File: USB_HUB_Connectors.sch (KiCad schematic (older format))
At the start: 52 parts

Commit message: Added footprint of 2x USB-A stacked. Added connections to USB HUB.
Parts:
- added D?: 1N4148WS, sc606-baseboard-footprints:SOD-323F, symbol sc606-baseboard:1N4148WS
- added FB?: BLM18EG221SN1D, sc606-baseboard-footprints:0603, symbol sc606-baseboard:BLM18EG221SN1D
- added TP? (x4): TP_SMD_0_75MM-antmicroTestPoints, sc606-baseboard-footprints:Testpoint_smd_0_75mm, symbol sc606-baseboard:TP_SMD_0_75MM-antmicroTestPoints
- added U? (x2): GSB3112311HR, sc606-baseboard-footprints:GSB3112311HR, symbol sc606-baseboard:GSB3112311HR
- C? (x2): footprint antmicro-footprints:0402-cap -> sc606-baseboard-footprints:0402-cap; symbol antmicroCapacitors0402:C_1u_0402 -> sc606-baseboard:C_1u_0402
- C? (x2): footprint antmicro-footprints:0402-cap -> sc606-baseboard-footprints:0402-cap; symbol antmicroCapacitors0402:C_10u_0402 -> sc606-baseboard:C_10u_0402
- R? (x5): footprint antmicro-footprints:0402-res -> sc606-baseboard-footprints:0402-res; symbol antmicroResistors0402:R_20k_0402 -> sc606-baseboard:R_20k_0402
- R?: footprint antmicro-footprints:0603-res -> sc606-baseboard-footprints:0603-res; symbol antmicroResistors0603:R_12k_1%_0603 -> sc606-baseboard:R_12k_1%_0603
- R?: footprint antmicro-footprints:0402-res -> sc606-baseboard-footprints:0402-res; symbol antmicroResistors0402:R_0R_0402 -> sc606-baseboard:R_0R_0402
- R?: footprint antmicro-footprints:0402-res -> sc606-baseboard-footprints:0402-res; symbol antmicroResistors0402:R_1M0_0402 -> sc606-baseboard:R_1M0_0402
- R? (x2): footprint antmicro-footprints:0402-res -> sc606-baseboard-footprints:0402-res; symbol antmicroResistors0402:R_200k_0402 -> sc606-baseboard:R_200k_0402
- TP?: footprint antmicro-footprints:Testpoint_smd_0_75mm -> sc606-baseboard-footprints:Testpoint_smd_0_75mm; symbol sc606-baseboard-rescue:TP_SMD_0_75MM-antmicroTestPoints -> sc606-baseboard:TP_SMD_0_75MM-antmicroTestPoints
- U?: footprint antmicro-footprints:QFN40P700X700X100-57N -> sc606-baseboard-footprints:QFN40P700X700X100-57N; symbol antmicroInterfaceControllers:USB57442G -> sc606-baseboard:USB57442G
- Y?: footprint antmicro-footprints:KX-7 -> sc606-baseboard-footprints:KX-7; symbol antmicroCrystals:ABM8G-25.000MHZ-B4Y-T -> sc606-baseboard:ABM8G-25.000MHZ-B4Y-T
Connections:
- net labels added: 5V0_SYS, 5V0_USB, USB_1_D_N, USB_1_D_P
- net labels removed: USBC_VBUS
- wire segments 143 -> 164
- no-connect marks 3 -> 1
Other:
- note added: "2x USB-A Stack connector"
- note added: "rozłożyć elementy na płytce i sprawdzić, czy dodamy drugi USB-C.\nWtedy trzeba robić switch.\nJak nie, to RX/TX2 podpinamy pod osobny port."
- moved on the sheet: C?, D?, J?, R?, TP?

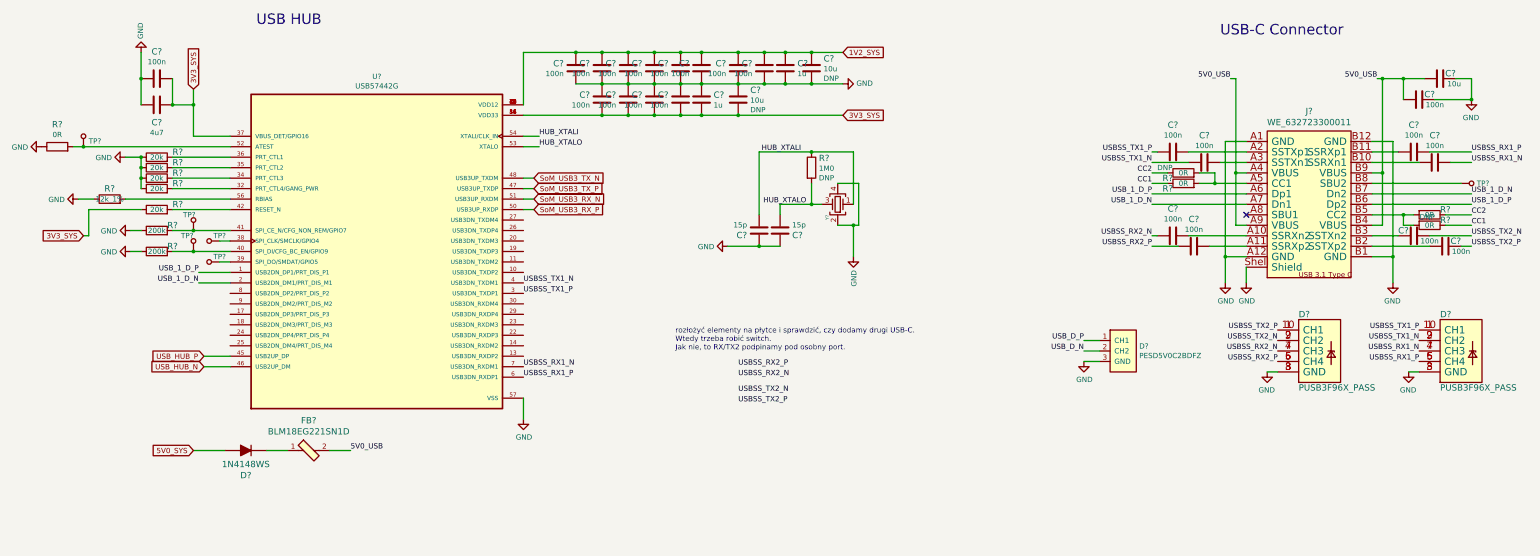
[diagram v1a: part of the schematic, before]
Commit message: Started placing main components on PCB. Change of RT battery model and USB flash connector
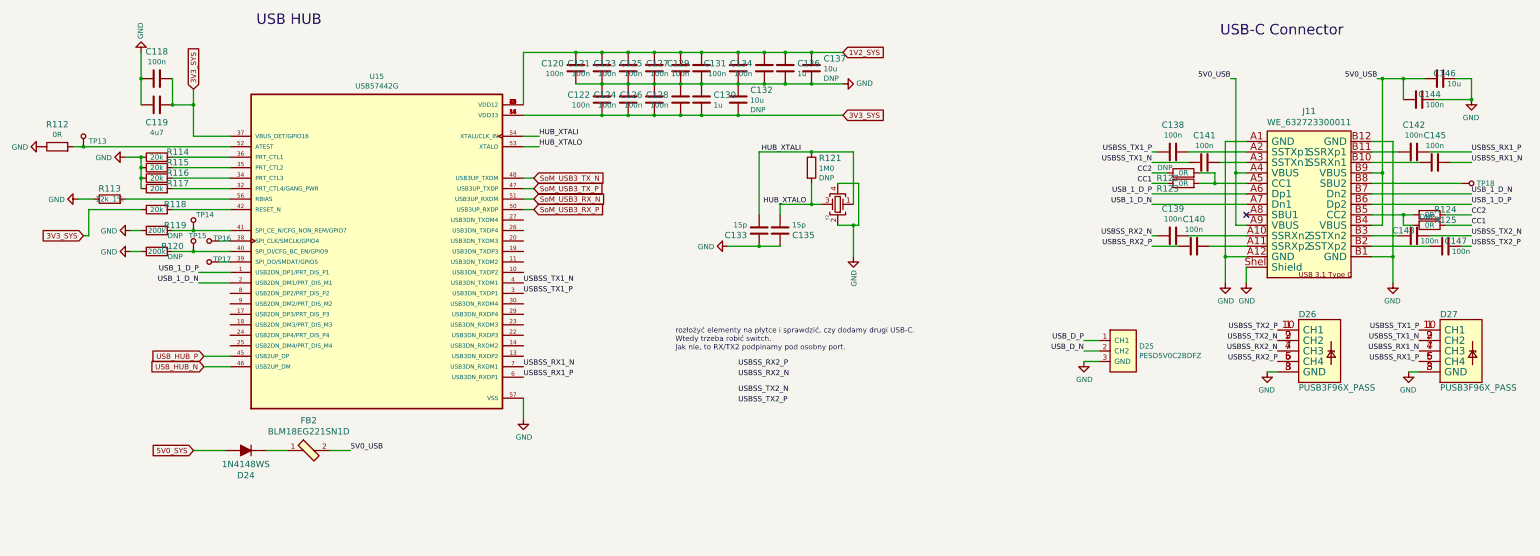
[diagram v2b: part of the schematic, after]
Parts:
- R119, R120: renamed from R?; DNP (none) -> DNP
- gave numbers to parts that had none: 57

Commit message: Added USB A and C double stack connector
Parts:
- removed C139, C140, C142, C143, C144, C145, C147: C_100n_0402, sc606-baseboard-footprints:0402-cap, symbol sc606-baseboard:C_100n_0402
- removed C146: C_10u_0402, sc606-baseboard-footprints:0402-cap, symbol sc606-baseboard:C_10u_0402
- removed J11: WE_632723300011, sc606-baseboard-footprints:WE_632723300011, symbol sc606-baseboard:WE_632723300011
- removed R124, R125: R_0R_0402, sc606-baseboard-footprints:0402-res, symbol sc606-baseboard:R_0R_0402
- removed TP18: TP_SMD_0_75MM, sc606-baseboard-footprints:Testpoint_smd_0_75mm, symbol sc606-baseboard:TP_SMD_0_75MM
- removed U14: GSB3112311HR, sc606-baseboard-footprints:GSB3112311HR, symbol sc606-baseboard:GSB3112311HR
- added C? (x7): C_100n_0402, sc606-baseboard-footprints:0402-cap, symbol sc606-baseboard:C_100n_0402
- added C?: C_10u_0402, sc606-baseboard-footprints:0402-cap, symbol sc606-baseboard:C_10u_0402
- added J? (x2): USB-A3-C31-D-RA-CS1, antmicro-footprints:USB-A3-C31-D-RA-CS1, symbol antmicroUSBDVIHDMIConnectors:USB-A3-C31-D-RA-CS1
- added R? (x2): R_0R_0402, sc606-baseboard-footprints:0402-res, symbol sc606-baseboard:R_0R_0402
- added TP? (x2): TP_SMD_0_75MM, sc606-baseboard-footprints:Testpoint_smd_0_75mm, symbol sc606-baseboard:TP_SMD_0_75MM
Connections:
- net labels added: USB_A1_D_N, USB_A1_D_P, USB_A1_SS_RX_N, USB_A1_SS_RX_P, USB_A1_SS_TX_N, USB_A1_SS_TX_P, USB_C1A_D_N, USB_C1A_D_P, USB_C1B_D_N, USB_C1B_D_P, USB_C1_CC1, USB_C1_CC2, USB_C1_SS_RX1_N, USB_C1_SS_RX1_P, USB_C1_SS_RX2_N, USB_C1_SS_RX2_P, USB_C1_SS_TX1_N, USB_C1_SS_TX1_P, USB_C1_SS_TX2_N, USB_C1_SS_TX2_P
- net labels removed: CC1, CC2
- wire segments 164 -> 153
- no-connect marks 1 -> 0
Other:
- note added: "2x USB-A and USB-C Stack connector"
- note removed: "2x USB-A Stack connector"
- note removed: "USB-C Connector"
- note removed: "rozłożyć elementy na płytce i sprawdzić, czy dodamy drugi USB-C.\nWtedy trzeba robić switch.\nJak nie, to RX/TX2 podpinamy pod osobny port."
- moved on the sheet: C138, C141, D25, D26, D27, R122, R123

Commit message: Added connections of both USB A & C connectors
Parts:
- removed D25: PESD5V0C2BDFZ, sc606-baseboard-footprints:DFN0603-3, symbol sc606-baseboard:PESD5V0C2BDFZ
- added C? (x11): C_100n_0402, sc606-baseboard-footprints:0402-cap, symbol sc606-baseboard:C_100n_0402
- added C? (x2): C_47u_0603, antmicro-footprints:0603-cap, symbol antmicroCapacitors0603:C_47u_0603
- added C?: C_10u_0402, sc606-baseboard-footprints:0402-cap, symbol sc606-baseboard:C_10u_0402
- added D? (x6): PUSB3F96X_PASS, sc606-baseboard-footprints:PUSB3F96X, symbol sc606-baseboard:PUSB3F96X_PASS
- added IC? (x2): HD3SS3220, antmicro-footprints:RNH0030A, symbol antmicroInterfaceControllers:HD3SS3220
- added J? (x2): USB-A3-C31-D-RA-CS1, antmicro-footprints:USB-A3-C31-D-RA-CS1, symbol antmicroUSBDVIHDMIConnectors:USB-A3-C31-D-RA-CS1
- added R? (x2): R_909k_0402, antmicro-footprints:0402-res, symbol antmicroResistors0402:R_909k_0402
- added R? (x4): R_200k_0402, antmicro-footprints:0402-res, symbol antmicroResistors0402:R_200k_0402
- added R? (x2): R_10k_0402, antmicro-footprints:0402-res, symbol antmicroResistors0402:R_10k_0402
- added R? (x6): R_2k_0402, antmicro-footprints:0402-res, symbol antmicroResistors0402:R_2k_0402
- added R? (x14): R_0R_0402, antmicro-footprints:0402-res, symbol antmicroResistors0402:R_0R_0402
- added R? (x4): R_0R_0402, sc606-baseboard-footprints:0402-res, symbol sc606-baseboard:R_0R_0402
- added TP? (x8): TP_SMD_0_75MM, sc606-baseboard-footprints:Testpoint_smd_0_75mm, symbol sc606-baseboard:TP_SMD_0_75MM
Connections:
- net USBSS_RX1_N is gone; now on net USB_C1_SS_TX2_P: D27.4 (CH3), D27.7 (CH3)
- net USBSS_RX1_P is gone; now on net USB_C1_SS_TX2_N: D27.5 (CH4), D27.6 (CH4)
- net USBSS_RX2_N is gone; now on net USB_A1_D_N: D26.4 (CH3), D26.7 (CH3)
- net USBSS_RX2_P is gone; now on net USB_A1_D_P: D26.5 (CH4), D26.6 (CH4)
- net USBSS_TX1_N is gone; now on net USB_C1_SS_RX2_N: D27.2 (CH2), D27.9 (CH2)
- net USBSS_TX1_P is gone; now on net USB_C1_SS_RX2_P: D27.1 (CH1), D27.10 (CH1)
- net USBSS_TX2_N is gone; now on net USB_C1_D_N: D26.2 (CH2), D26.9 (CH2)
- net USBSS_TX2_P is gone; now on net USB_C1_D_P: D26.1 (CH1), D26.10 (CH1)
- net USB_1_D_N is gone; now on net USB_A1_D_N: U15.2 (USB2DN_DM1/PRT_DIS_M1)
- net USB_1_D_P is gone; now on net USB_A1_D_P: U15.1 (USB2DN_DP1/PRT_DIS_P1)
- net USB_C1A_D_N is gone; now on net USB_C1_D_N: J?.A7 (DA-)
- net USB_C1A_D_P is gone; now on net USB_C1_D_P: J?.A6 (DA+)
- net USB_C1B_D_N is gone; now on net USB_C1_D_N: J?.B7 (DB-)
- net USB_C1B_D_P is gone; now on net USB_C1_D_P: J?.B6 (DB+)
- net 3V3_SYS: now also C?.2, C?.2, IC?.8 (VCC33), IC?.8 (VCC33), R?.1, R?.1, R?.1, R?.1, R?.2, R?.2
- net 5V0_SYS: now also C?.1, C?.1, IC?.30 (VDD5), IC?.30 (VDD5), R?.1, R?.1, R?.1, R?.1, R?.1, R?.1
- net 5V0_USB: now also C?.1, C?.2, J?.1 (VBUS), J?.A4 (VBUS), J?.A9 (VBUS), J?.B4 (VBUS), J?.B9 (VBUS), R?.1, R?.1
- net GND: now also C?.1, C?.1, C?.1, C?.2, C?.2, C?.2, D?.3 (GND), D?.3 (GND), D?.3 (GND), D?.3 (GND), D?.3 (GND), D?.3 (GND), D?.8 (GND), D?.8 (GND), D?.8 (GND), D?.8 (GND), D?.8 (GND), D?.8 (GND), IC?.13 (GND), IC?.13 (GND), IC?.28 (GND), IC?.28 (GND), IC?.31 (GND), IC?.31 (GND), J?.4 (GND), J?.7 (GNDDRAIN), J?.A1 (GND), J?.A12 (GND), J?.B1 (GND), J?.B12 (GND), R?.1, R?.1, R?.1, R?.1
- net SoM_USB3_RX_N: now also U15.48 (USB3UP_TXDM); no longer U15.51 (USB3UP_RXDM)
- net SoM_USB3_RX_P: now also U15.47 (USB3UP_TXDP); no longer U15.50 (USB3UP_RXDP)
- net SoM_USB3_TX_N: now also U15.51 (USB3UP_RXDM); no longer U15.48 (USB3UP_TXDM)
- net SoM_USB3_TX_P: now also U15.50 (USB3UP_RXDP); no longer U15.47 (USB3UP_TXDP)
- net USB_A1_SS_RX_N: now also U15.7 (USB3DN_RXDM1), D?.5 (CH4), D?.6 (CH4)
- net USB_A1_SS_RX_P: now also U15.6 (USB3DN_RXDP1), D?.4 (CH3), D?.7 (CH3)
- net USB_A1_SS_TX_N: now also U15.4 (USB3DN_TXDM1), D?.2 (CH2), D?.9 (CH2)
- net USB_A1_SS_TX_P: now also U15.3 (USB3DN_TXDP1), D?.1 (CH1), D?.10 (CH1)
- net USB_C1_CC1: now also IC?.2 (CC1)
- net USB_C1_CC2: now also IC?.1 (CC2)
- net USB_C1_SS_RX1_N: now also D?.5 (CH4), D?.6 (CH4), IC?.14 (RX1n)
- net USB_C1_SS_RX1_P: now also D?.4 (CH3), D?.7 (CH3), IC?.15 (RX1p)
- net USB_C1_SS_RX2_N: now also IC?.18 (RX2n)
- net USB_C1_SS_RX2_P: now also IC?.19 (RX2p)
- net USB_C1_SS_TX1_N: now also D?.2 (CH2), D?.9 (CH2), IC?.16 (TX1n)
- net USB_C1_SS_TX1_P: now also D?.1 (CH1), D?.10 (CH1), IC?.17 (TX1p)
- net USB_C1_SS_TX2_N: now also IC?.20 (TX2n)
- net USB_C1_SS_TX2_P: now also IC?.21 (TX2p)
- net USB_C1_SS_TX_P: now reaches U15.10 (USB3DN_TXDP2)
- net USB_C1_SS_TX_P: now also R?.1
- net USB_C1_SS_TX_N: now reaches U15.11 (USB3DN_TXDM2)
- net USB_C1_SS_TX_N: now also R?.1
- net USB_C1_SS_RX_P: now reaches U15.13 (USB3DN_RXDP2)
- net USB_C1_SS_RX_P: now also R?.1
- net USB_C1_SS_RX_N: now reaches U15.14 (USB3DN_RXDM2)
- net USB_C1_SS_RX_N: now also R?.1
- net USB_A2_D_P: now reaches U15.17 (USB2DN_DP3/PRT_DIS_P3)
- net USB_A2_D_P: now also D?.5 (CH4), D?.6 (CH4), J?.3 (D+)
- net USB_A2_D_N: now reaches U15.18 (USB2DN_DM3/PRT_DIS_M3)
- net USB_A2_D_N: now also D?.4 (CH3), D?.7 (CH3), J?.2 (D-)
- net USB_A2_SS_TX_P: now reaches U15.19 (USB3DN_TXDP3)
- net USB_A2_SS_TX_P: now also D?.1 (CH1), D?.10 (CH1), J?.9 (STDA_SSTX+)
- net USB_A2_SS_TX_N: now reaches U15.20 (USB3DN_TXDM3)
- net USB_A2_SS_TX_N: now also D?.2 (CH2), D?.9 (CH2), J?.8 (STDA_SSTX-)
- net USB_A2_SS_RX_P: now reaches U15.22 (USB3DN_RXDP3)
- net USB_A2_SS_RX_P: now also D?.4 (CH3), D?.7 (CH3), J?.6 (STDA_SSRX+)
- net USB_A2_SS_RX_N: now reaches U15.23 (USB3DN_RXDM3)
- net USB_A2_SS_RX_N: now also D?.5 (CH4), D?.6 (CH4), J?.5 (STDA_SSRX-)
- net USB_C2_D_P: now reaches U15.24 (USB2DN_DP4/PRT_DIS_P4)
- net USB_C2_D_P: now also D?.1 (CH1), D?.10 (CH1), J?.A6 (DA+), J?.B6 (DB+)
- net USB_C2_D_N: now reaches U15.25 (USB2DN_DM4/PRT_DIS_M4)
- net USB_C2_D_N: now also D?.2 (CH2), D?.9 (CH2), J?.A7 (DA-), J?.B7 (DB-)
- net USB_C2_SS_TX_P: now reaches U15.26 (USB3DN_TXDP4)
- net USB_C2_SS_TX_P: now also R?.1
- net USB_C2_SS_TX_N: now reaches U15.27 (USB3DN_TXDM4)
- net USB_C2_SS_TX_N: now also R?.1
- net USB_C2_SS_RX_P: now reaches U15.29 (USB3DN_RXDP4)
- net USB_C2_SS_RX_P: now also R?.1
- net USB_C2_SS_RX_N: now reaches U15.30 (USB3DN_RXDM4)
- net USB_C2_SS_RX_N: now also R?.1
- net USB_C1_D_P: now reaches U15.8 (USB2DN_DP2/PRT_DIS_P2)
- net USB_C1_D_N: now reaches U15.9 (USB2DN_DM2/PRT_DIS_M2)
- new net: IC?.10 (RXn), R?.2 (x2)
- new net: IC?.11 (DIR), R?.1 (x2)
- new net: IC?.22 (ADDR), TP?.1 (x2)
- new net: IC?.23 (INT_N/OUT3), R?.2 (x2)
- new net: IC?.24 (VCONN_FAULT_N), TP?.1 (x2)
- new net: IC?.25 (SDA/OUT1), R?.2 (x2)
- new net: IC?.26 (SCL/OUT2), R?.2 (x2)
- new net: IC?.29 (ENn_CC), R?.2 (x2)
- new net: IC?.3 (CURRENT_MODE), R?.2 (x2)
- new net: IC?.4 (PORT), R?.2 (x2)
- new net: IC?.5 (VBUS_DET), R?.2 (x2)
- new net: IC?.6 (TXp), R?.2 (x2)
- new net: IC?.7 (TXn), R?.2 (x2)
- new net: IC?.9 (RXp), R?.2 (x2)
- new net: J?.B5 (CC2), R?.2, R?.2
- new net: C?.1, J?.A2 (TX1+)
- new net: C?.1, J?.A3 (TX1-)
- new net: C?.1, J?.A10 (RX2-)
- new net: C?.1, J?.A11 (RX2+)
- new net: J?.A5 (CC1), R?.2, R?.2
- new net: J?.A8 (SBU1), TP?.1
- new net: C?.1, J?.B10 (RX1-)
- new net: C?.1, J?.B11 (RX1+)
- new net: C?.1, J?.B2 (TX2+)
- new net: C?.1, J?.B3 (TX2-)
- new net: J?.B8 (SBU2), TP?.1
- new net EN1_MUX: IC?.12 (ENn_MUX), R?.1, R?.2
- new net EN2_MUX: IC?.12 (ENn_MUX), R?.1, R?.2
- new net USBC1_ID: IC?.27 (ID), R?.2, TP?.1
- new net USBC2_ID: IC?.27 (ID), R?.2, TP?.1
- new net USB_C2_CC1: IC?.2 (CC1), R?.1, R?.1
- new net USB_C2_CC2: IC?.1 (CC2), R?.1, R?.1
- new net USB_C2_SS_RX1_N: C?.2, D?.5 (CH4), D?.6 (CH4), IC?.14 (RX1n)
- new net USB_C2_SS_RX1_P: C?.2, D?.4 (CH3), D?.7 (CH3), IC?.15 (RX1p)
- new net USB_C2_SS_RX2_N: C?.2, D?.2 (CH2), D?.9 (CH2), IC?.18 (RX2n)
- new net USB_C2_SS_RX2_P: C?.2, D?.1 (CH1), D?.10 (CH1), IC?.19 (RX2p)
- new net USB_C2_SS_TX1_N: C?.2, D?.2 (CH2), D?.9 (CH2), IC?.16 (TX1n)
- new net USB_C2_SS_TX1_P: C?.2, D?.1 (CH1), D?.10 (CH1), IC?.17 (TX1p)
- new net USB_C2_SS_TX2_N: C?.2, D?.5 (CH4), D?.6 (CH4), IC?.20 (TX2n)
- new net USB_C2_SS_TX2_P: C?.2, D?.4 (CH3), D?.7 (CH3), IC?.21 (TX2p)
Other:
- note added: "USB-A and USB-C Stack connector"
- note removed: "2x USB-A and USB-C Stack connector"
- moved on the sheet: C138, C141, C?, D26, D27, J?A, J?B, R122, R123, R?, TP?

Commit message: Main components placed on board
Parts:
- gave numbers to parts that had none: 76

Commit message: Main 5V buck converter placed and routed
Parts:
- C146, C158: footprint antmicro-footprints:0603-cap -> sc606-baseboard-footprints:0603-cap; symbol antmicroCapacitors0603:C_47u_0603 -> sc606-baseboard:C_47u_0603
- IC3, IC4: footprint antmicro-footprints:RNH0030A -> sc606-baseboard-footprints:RNH0030A; symbol antmicroInterfaceControllers:HD3SS3220 -> sc606-baseboard:HD3SS3220
- J11, J13: footprint antmicro-footprints:USB-A3-C31-D-RA-CS1 -> sc606-baseboard-footprints:USB-A3-C31-D-RA-CS1; symbol antmicroUSBDVIHDMIConnectors:USB-A3-C31-D-RA-CS1 -> sc606-baseboard:USB-A3-C31-D-RA-CS1
- R130, R142, R144, R160: footprint antmicro-footprints:0402-res -> sc606-baseboard-footprints:0402-res; symbol antmicroResistors0402:R_200k_0402 -> sc606-baseboard:R_200k_0402
- R131, R145: footprint antmicro-footprints:0402-res -> sc606-baseboard-footprints:0402-res; symbol antmicroResistors0402:R_10k_0402 -> sc606-baseboard:R_10k_0402
- R132, R139, R140, R146, R153, R154: footprint antmicro-footprints:0402-res -> sc606-baseboard-footprints:0402-res; symbol antmicroResistors0402:R_2k_0402 -> sc606-baseboard:R_2k_0402
- R133, R134, R135, R136, R137, R138, R143, R147, R148, R149, R150, R151, R152, R161: footprint antmicro-footprints:0402-res -> sc606-baseboard-footprints:0402-res; symbol antmicroResistors0402:R_0R_0402 -> sc606-baseboard:R_0R_0402
- R141, R159: footprint antmicro-footprints:0402-res -> sc606-baseboard-footprints:0402-res; symbol antmicroResistors0402:R_909k_0402 -> sc606-baseboard:R_909k_0402

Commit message: FFC and general display camera connectors distributed on board
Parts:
- added C159, C160, C161, C162, C163, C164, C165, C166: C_100n_0402, sc606-baseboard-footprints:0402-cap, symbol sc606-baseboard:C_100n_0402
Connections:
- net USB_A1_SS_RX_N: now also C159.2; no longer J11.5 (STDA_SSRX-)
- net USB_A1_SS_RX_P: now also C161.2; no longer J11.6 (STDA_SSRX+)
- net USB_A1_SS_TX_N: now also C160.2; no longer J11.8 (STDA_SSTX-)
- net USB_A1_SS_TX_P: now also C162.2; no longer J11.9 (STDA_SSTX+)
- net USB_A2_SS_RX_N: now also C163.2; no longer J13.5 (STDA_SSRX-)
- net USB_A2_SS_RX_P: now also C165.2; no longer J13.6 (STDA_SSRX+)
- net USB_A2_SS_TX_N: now also C164.2; no longer J13.8 (STDA_SSTX-)
- net USB_A2_SS_TX_P: now also C166.2; no longer J13.9 (STDA_SSTX+)
- net USB_C1_SS_C_TX1_P: now reaches C138.1, J11.A2 (TX1+)
- net USB_C1_SS_C_TX1_N: now reaches C141.1, J11.A3 (TX1-)
- net USB_C1_SS_C_TX2_P: now reaches C94.1, J11.B2 (TX2+)
- net USB_C1_SS_C_TX2_N: now reaches C102.1, J11.B3 (TX2-)
- net USB_C1_SS_C_RX_N: now reaches IC3.10 (RXn), R138.2
- net USB_C1_SS_C_TX_P: now reaches IC3.6 (TXp), R135.2
- net USB_C1_SS_C_TX_N: now reaches IC3.7 (TXn), R136.2
- net USB_C1_SS_C_RX_P: now reaches IC3.9 (RXp), R137.2
- net USB_C2_SS_C_TX1_P: now reaches C147.1, J13.A2 (TX1+)
- net USB_C2_SS_C_TX1_N: now reaches C149.1, J13.A3 (TX1-)
- net USB_C2_SS_C_RX2_N: now reaches C153.1, J13.A10 (RX2-)
- net USB_C2_SS_C_RX2_P: now reaches C155.1, J13.A11 (RX2+)
- net USB_C2_SS_C_RX1_N: now reaches C154.1, J13.B10 (RX1-)
- net USB_C2_SS_C_RX1_P: now reaches C156.1, J13.B11 (RX1+)
- net USB_C2_SS_C_TX2_P: now reaches C148.1, J13.B2 (TX2+)
- net USB_C2_SS_C_TX2_N: now reaches C150.1, J13.B3 (TX2-)
- net USB_C2_SS_C_RX_N: now reaches IC4.10 (RXn), R152.2
- net USB_C2_SS_C_TX_P: now reaches IC4.6 (TXp), R149.2
- net USB_C2_SS_C_TX_N: now reaches IC4.7 (TXn), R150.2
- net USB_C2_SS_C_RX_P: now reaches IC4.9 (RXp), R151.2
- new net USB_A1_SS_C_RX_N: C159.1, J11.5 (STDA_SSRX-)
- new net USB_A1_SS_C_RX_P: C161.1, J11.6 (STDA_SSRX+)
- new net USB_A1_SS_C_TX_N: C160.1, J11.8 (STDA_SSTX-)
- new net USB_A1_SS_C_TX_P: C162.1, J11.9 (STDA_SSTX+)
- new net USB_A2_SS_C_RX_N: C163.1, J13.5 (STDA_SSRX-)
- new net USB_A2_SS_C_RX_P: C165.1, J13.6 (STDA_SSRX+)
- new net USB_A2_SS_C_TX_N: C164.1, J13.8 (STDA_SSTX-)
- new net USB_A2_SS_C_TX_P: C166.1, J13.9 (STDA_SSTX+)
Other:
- moved on the sheet: C102, C103, C133, C135, C138, C139, C140, C141, C142, C143, C144, C145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
